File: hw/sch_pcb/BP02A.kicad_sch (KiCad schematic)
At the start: 38 parts, among them J1 SATA7-67491-1030, J2 SATA7-67491-1030, M1 HOLE, M2 HOLE, M3 HOLE, M4 HOLE

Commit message: Updated parts specification. #2
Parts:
- C1, C10, C11, C12, C13, C2, C3, C4: UST_ID (none) -> 5c70984712875079b91f8b3b
- C5, C7, C9: UST_ID (none) -> 5c70984712875079b91f8b33
- C6: UST_ID (none) -> 5c70984712875079b91f8b37
- C8: UST_ID (none) -> 5dad549f128750448eca1926
- J1, J2: UST_ID (none) -> 5c70984712875079b91f8a7b
- L1, L18, L19, L2: UST_ID (none) -> 5c70984412875079b91f8807
- L10, L9: MFPN 0805AS-027J-08 -> CW0805-39; UST_ID (none) -> 5c70984412875079b91f8809
- L11, L17, L5: MFPN CW0805-15 -> CW0805-10; UST_ID (none) -> 60be72061287500165e6c35e
- L12: MFPN 0805AS-027J-08 -> (none); UST_ID (none) -> 5fa100d812875025b39779cf
- L13, L14, L7, L8: MFPN CW0805-12 -> CW0805-82; UST_ID (none) -> 60be7e351287500165e6c39b
- L15, L16: MFPN 0805AS-027J-08 -> CW0805-18; UST_ID (none) -> 5c70984412875079b91f8806
- L3, L4: UST_ID (none) -> 60be80ed1287500165e6c3bb
- L6: MFPN 0805AS-027J-08 -> (none); UST_ID (none) -> 5c70984412875079b91f8803
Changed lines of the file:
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@@
+      (effects (font (size 1.27 1.27)) hide)
+    )
+    (property "UST_ID" "5c70984412875079b91f8807" (id 5) (at 110.49 71.12 0)
       (effects (font (size 1.27 1.27)) hide)
     )
@@
       (effects (font (size 1.27 1.27)) hide)
     )
+    (property "UST_ID" "5c70984412875079b91f8807" (id 5) (at 110.49 83.82 0)
+      (effects (font (size 1.27 1.27)) hide)
+    )
     (pin "1")
     (pin "2")
@@
       (effects (font (size 1.27 1.27)) hide)
     )
+    (property "UST_ID" "60be80ed1287500165e6c3bb" (id 5) (at 118.11 107.315 0)
+      (effects (font (size 1.27 1.27)) hide)
+    )
     (pin "1")
     (pin "2")
@@
       (effects (font (size 1.27 1.27)) hide)
     )
+    (property "UST_ID" "60be80ed1287500165e6c3bb" (id 5) (at 118.11 120.015 0)
+      (effects (font (size 1.27 1.27)) hide)
+    )
     (pin "1")
     (pin "2")
@@
       (effects (font (size 1.27 1.27)) hide)
     )
-    (property "MFPN" "CW0805-15" (id 4) (at 122.555 77.47 90)
+    (property "MFPN" "CW0805-10" (id 4) (at 122.555 77.47 90)
+      (effects (font (size 1.27 1.27)) hide)
+    )
+    (property "UST_ID" "60be72061287500165e6c35e" (id 5) (at 122.555 77.47 0)
       (effects (font (size 1.27 1.27)) hide)
     )
@@
       (effects (font (size 1.27 1.27)) hide)
     )
-    (property "MFPN" "0805AS-027J-08" (id 4) (at 129.54 113.665 90)
+    (property "MFPN" "" (id 4) (at 129.54 113.665 90)
+      (effects (font (size 1.27 1.27)) hide)
+    )
+    (property "UST_ID" "5c70984412875079b91f8803" (id 5) (at 129.54 113.665 0)
       (effects (font (size 1.27 1.27)) hide)
     )
@@
       (effects (font (size 1.27 1.27)) hide)
     )
-    (property "MFPN" "CW0805-12" (id 4) (at 130.175 71.12 90)
+    (property "MFPN" "CW0805-82" (id 4) (at 130.175 71.12 90)
+      (effects (font (size 1.27 1.27)) hide)
+    )
+    (property "UST_ID" "60be7e351287500165e6c39b" (id 5) (at 130.175 71.12 0)
       (effects (font (size 1.27 1.27)) hide)
     )
@@
       (effects (font (size 1.27 1.27)) hide)
     )
-    (property "MFPN" "CW0805-12" (id 4) (at 130.175 83.82 90)
+    (property "MFPN" "CW0805-82" (id 4) (at 130.175 83.82 90)
+      (effects (font (size 1.27 1.27)) hide)
+    )
+    (property "UST_ID" "60be7e351287500165e6c39b" (id 5) (at 130.175 83.82 0)
       (effects (font (size 1.27 1.27)) hide)
     )
@@
       (effects (font (size 1.27 1.27)) hide)
     )
-    (property "MFPN" "0805AS-027J-08" (id 4) (at 140.335 107.315 90)
+    (property "MFPN" " CW0805-39" (id 4) (at 140.335 107.315 90)
+      (effects (font (size 1.27 1.27)) hide)
+    )
+    (property "UST_ID" "5c70984412875079b91f8809" (id 5) (at 140.335 107.315 0)
       (effects (font (size 1.27 1.27)) hide)
     )
@@
       (effects (font (size 1.27 1.27)) hide)
     )
-    (property "MFPN" "0805AS-027J-08" (id 4) (at 140.335 120.015 90)
+    (property "MFPN" " CW0805-39" (id 4) (at 140.335 120.015 90)
+      (effects (font (size 1.27 1.27)) hide)
+    )
+    (property "UST_ID" "5c70984412875079b91f8809" (id 5) (at 140.335 120.015 0)
       (effects (font (size 1.27 1.27)) hide)
     )
@@
       (effects (font (size 1.27 1.27)) hide)
     )
-    (property "MFPN" "CW0805-15" (id 4) (at 144.145 77.47 90)
+    (property "MFPN" "CW0805-10" (id 4) (at 144.145 77.47 90)
+      (effects (font (size 1.27 1.27)) hide)
+    )
+    (property "UST_ID" "60be72061287500165e6c35e" (id 5) (at 144.145 77.47 0)
       (effects (font (size 1.27 1.27)) hide)
     )
@@
       (effects (font (size 1.27 1.27)) hide)
     )
-    (property "MFPN" "0805AS-027J-08" (id 4) (at 151.765 113.665 90)
+    (property "MFPN" "" (id 4) (at 151.765 113.665 90)
+      (effects (font (size 1.27 1.27)) hide)
+    )
+    (property "UST_ID" "5fa100d812875025b39779cf" (id 5) (at 151.765 113.665 0)
       (effects (font (size 1.27 1.27)) hide)
     )
@@
       (effects (font (size 1.27 1.27)) hide)
     )
-    (property "MFPN" "CW0805-12" (id 4) (at 154.94 71.12 90)
+    (property "MFPN" "CW0805-82" (id 4) (at 154.94 71.12 90)
+      (effects (font (size 1.27 1.27)) hide)
+    )
+    (property "UST_ID" "60be7e351287500165e6c39b" (id 5) (at 154.94 71.12 0)
       (effects (font (size 1.27 1.27)) hide)
     )
@@
       (effects (font (size 1.27 1.27)) hide)
     )
-    (property "MFPN" "CW0805-12" (id 4) (at 154.94 83.82 90)
+    (property "MFPN" "CW0805-82" (id 4) (at 154.94 83.82 90)
+      (effects (font (size 1.27 1.27)) hide)
+    )
+    (property "UST_ID" "60be7e351287500165e6c39b" (id 5) (at 154.94 83.82 0)
       (effects (font (size 1.27 1.27)) hide)
     )
@@
       (effects (font (size 1.27 1.27)) hide)
     )
-    (property "MFPN" "0805AS-027J-08" (id 4) (at 162.56 107.315 90)
+    (property "MFPN" "CW0805-18" (id 4) (at 162.56 107.315 90)
+      (effects (font (size 1.27 1.27)) hide)
+    )
+    (property "UST_ID" "5c70984412875079b91f8806" (id 5) (at 162.56 107.315 0)
       (effects (font (size 1.27 1.27)) hide)
     )
@@
       (effects (font (size 1.27 1.27)) hide)
     )
-    (property "MFPN" "0805AS-027J-08" (id 4) (at 162.56 120.015 90)
+    (property "MFPN" "CW0805-18" (id 4) (at 162.56 120.015 90)
+      (effects (font (size 1.27 1.27)) hide)
+    )
+    (property "UST_ID" "5c70984412875079b91f8806" (id 5) (at 162.56 120.015 0)
       (effects (font (size 1.27 1.27)) hide)
     )
@@
       (effects (font (size 1.27 1.27)) hide)
     )
-    (property "MFPN" "CW0805-15" (id 4) (at 170.815 77.47 90)
+    (property "MFPN" "CW0805-10" (id 4) (at 170.815 77.47 90)
+      (effects (font (size 1.27 1.27)) hide)
+    )
+    (property "UST_ID" "60be72061287500165e6c35e" (id 5) (at 170.815 77.47 0)
       (effects (font (size 1.27 1.27)) hide)
     )
@@
       (effects (font (size 1.27 1.27)) hide)
     )
+    (property "UST_ID" "5c70984412875079b91f8807" (id 5) (at 178.435 71.12 0)
+      (effects (font (size 1.27 1.27)) hide)
+    )
     (pin "1")
     (pin "2")
@@
       (effects (font (size 1.27 1.27)) hide)
     )
+    (property "UST_ID" "5c70984412875079b91f8807" (id 5) (at 178.435 83.82 0)
+      (effects (font (size 1.27 1.27)) hide)
+    )
     (pin "1")
     (pin "2")
@@
       (effects (font (size 1.524 1.524)))
     )
+    (property "UST_ID" "5c70984712875079b91f8b3b" (id 4) (at 102.87 71.12 0)
+      (effects (font (size 1.27 1.27)) hide)
+    )
     (pin "1")
     (pin "2")
@@
       (effects (font (size 1.524 1.524)))
     )
+    (property "UST_ID" "5c70984712875079b91f8b3b" (id 4) (at 102.87 83.82 0)
+      (effects (font (size 1.27 1.27)) hide)
+    )
     (pin "1")
     (pin "2")
@@
       (effects (font (size 1.524 1.524)))
     )
+    (property "UST_ID" "5c70984712875079b91f8b3b" (id 4) (at 108.585 107.315 0)
+      (effects (font (size 1.27 1.27)) hide)
+    )
     (pin "1")
     (pin "2")
@@
       (effects (font (size 1.524 1.524)))
     )
+    (property "UST_ID" "5c70984712875079b91f8b3b" (id 4) (at 108.585 120.015 0)
+      (effects (font (size 1.27 1.27)) hide)
+    )
     (pin "1")
     (pin "2")
@@
       (effects (font (size 1.524 1.524)))
     )
+    (property "UST_ID" "5c70984712875079b91f8b33" (id 4) (at 117.475 77.47 0)
+      (effects (font (size 1.27 1.27)) hide)
+    )
     (pin "1")
     (pin "2")
@@
       (effects (font (size 1.524 1.524)))
     )
+    (property "UST_ID" "5c70984712875079b91f8b37" (id 4) (at 126.365 113.665 0)
+      (effects (font (size 1.27 1.27)) hide)
+    )
     (pin "1")
     (pin "2")
@@
       (effects (font (size 1.524 1.524)))
     )
+    (property "UST_ID" "5c70984712875079b91f8b33" (id 4) (at 139.065 77.47 0)
+      (effects (font (size 1.27 1.27)) hide)
+    )
     (pin "1")
     (pin "2")
@@
       (effects (font (size 1.524 1.524)))
     )
+    (property "UST_ID" "5dad549f128750448eca1926" (id 4) (at 147.955 113.665 0)
+      (effects (font (size 1.27 1.27)) hide)
+    )
     (pin "1")
     (pin "2")
@@
       (effects (font (size 1.524 1.524)))
     )
+    (property "UST_ID" "5c70984712875079b91f8b33" (id 4) (at 167.005 77.47 0)
+      (effects (font (size 1.27 1.27)) hide)
+    )
     (pin "1")
     (pin "2")
@@
       (effects (font (size 1.524 1.524)))
     )
+    (property "UST_ID" "5c70984712875079b91f8b3b" (id 4) (at 172.085 107.315 0)
+      (effects (font (size 1.27 1.27)) hide)
+    )
     (pin "1")
     (pin "2")
@@
       (effects (font (size 1.524 1.524)))
     )
+    (property "UST_ID" "5c70984712875079b91f8b3b" (id 4) (at 172.085 120.015 0)
+      (effects (font (size 1.27 1.27)) hide)
+    )
     (pin "1")
     (pin "2")
@@
       (effects (font (size 1.524 1.524)))
     )
+    (property "UST_ID" "5c70984712875079b91f8b3b" (id 4) (at 187.325 71.12 0)
+      (effects (font (size 1.27 1.27)) hide)
+    )
     (pin "1")
     (pin "2")
@@
     (property "Datasheet" "" (id 3) (at 187.325 83.82 0)
       (effects (font (size 1.524 1.524)))
+    )
+    (property "UST_ID" "5c70984712875079b91f8b3b" (id 4) (at 187.325 83.82 0)
+      (effects (font (size 1.27 1.27)) hide)
     )
     (pin "1")
@@
     (property "Datasheet" "" (id 3) (at 34.29 97.79 0)
       (effects (font (size 1.524 1.524)))
+    )
+    (property "UST_ID" "5c70984712875079b91f8a7b" (id 4) (at 34.29 97.79 0)
+      (effects (font (size 1.27 1.27)) hide)
     )
     (pin "1")
@@
       (effects (font (size 1.524 1.524)))
     )
-    (pin "1")
+    (property "UST_ID" "5c70984712875079b91f8a7b" (id 4) (at 251.46 99.695 0)
+      (effects (font (size 1.27 1.27)) hide)
+    )
+    (pin "1")

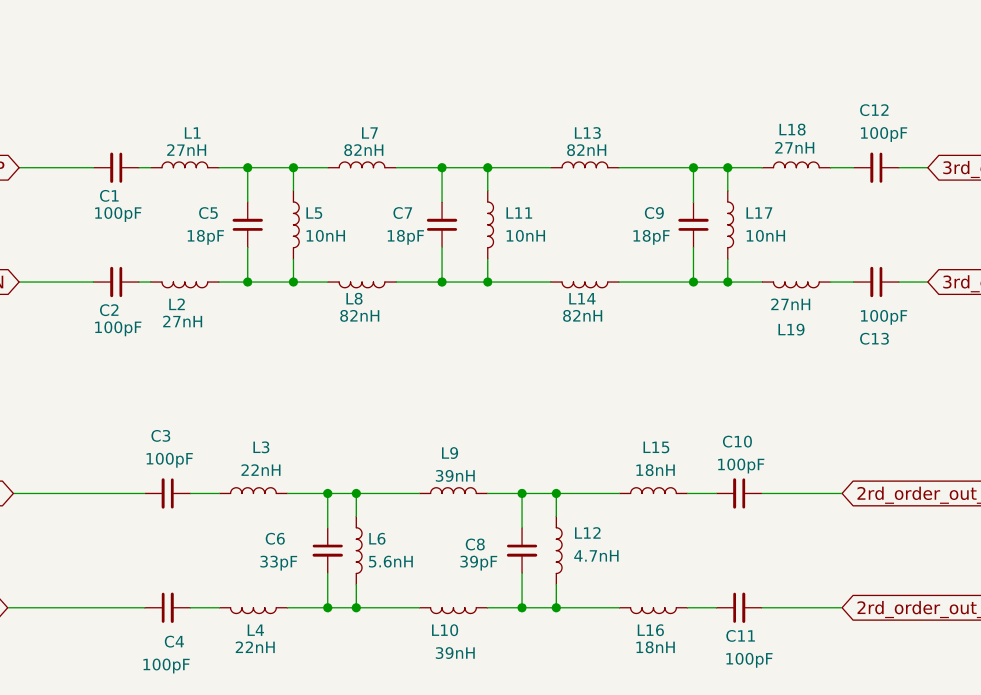
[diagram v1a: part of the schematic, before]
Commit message: exchanged multilayer inductor by wire wound.
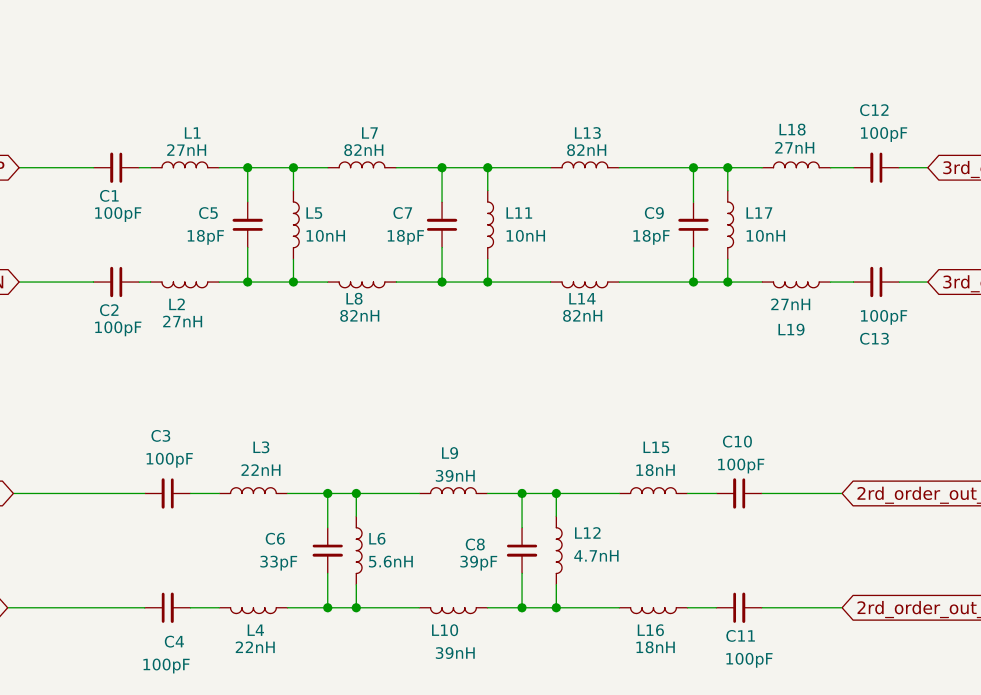
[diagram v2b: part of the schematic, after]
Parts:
- L12: UST_ID 5fa100d812875025b39779cf -> 60d330e0128750016518ca90
